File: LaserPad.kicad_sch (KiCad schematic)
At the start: 0 parts

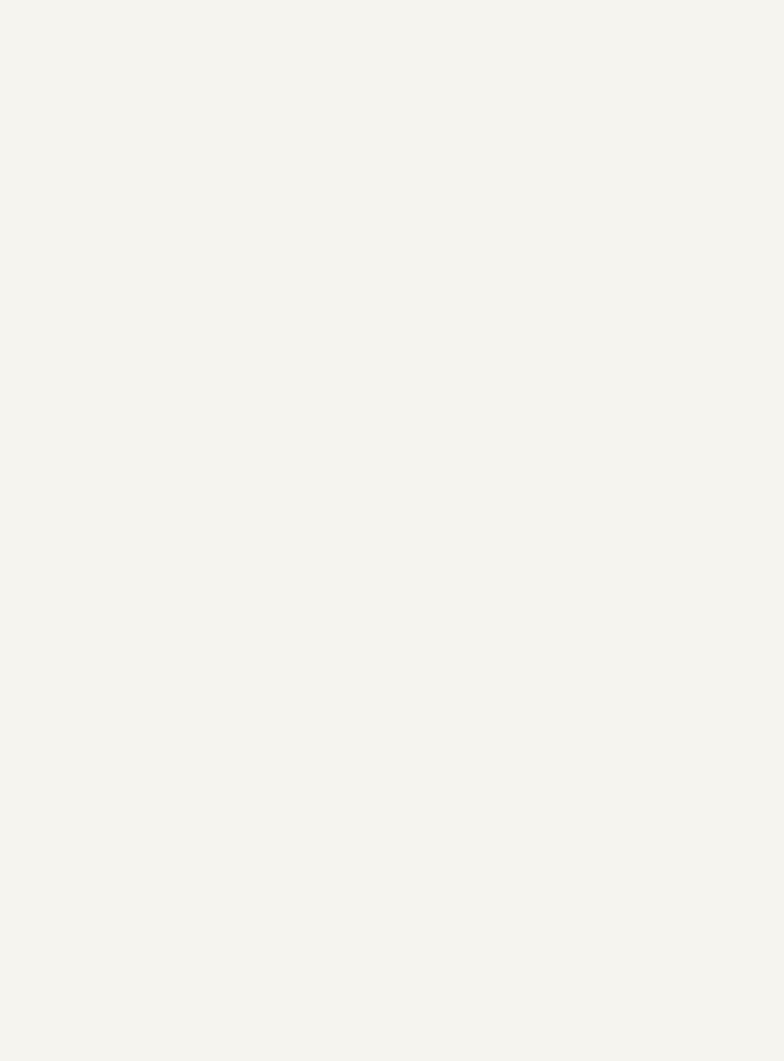
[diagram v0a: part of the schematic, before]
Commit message: Selected MCU and wired up RGB Led Underglow
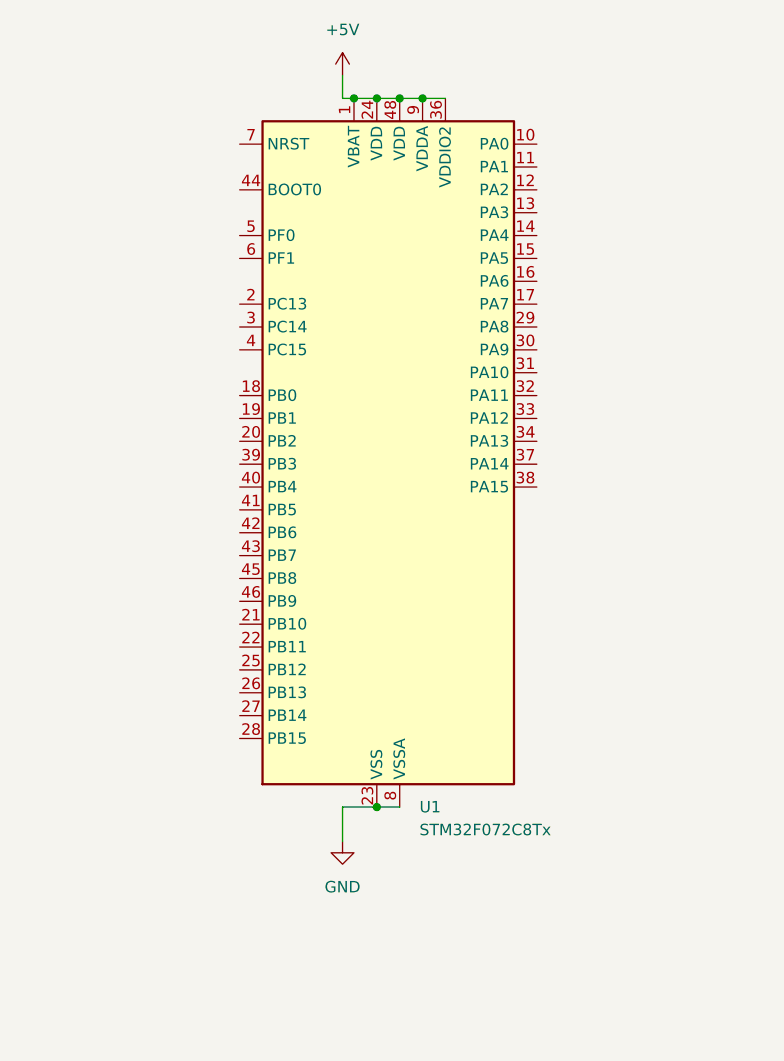
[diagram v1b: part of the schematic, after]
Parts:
- added U1: STM32F072C8Tx, Package_QFP:LQFP-48_7x7mm_P0.5mm, symbol MCU_ST_STM32F0:STM32F072C8Tx
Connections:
- new net +5V: U1.1 (VBAT), U1.24 (VDD), U1.36 (VDDIO2), U1.48 (VDD), U1.9 (VDDA)
- new net GND: U1.23 (VSS), U1.35 (VSS), U1.47 (VSS), U1.8 (VSSA)
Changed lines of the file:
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@@
 (kicad_sch (version 20230121) (generator eeschema)
   (paper "A4")
+  (junction (at 132.08 40.64) (diameter 0) (color 0 0 0 0)
+  )
+  (junction (at 127 119.38) (diameter 0) (color 0 0 0 0)
+  )
+  (junction (at 124.46 40.64) (diameter 0) (color 0 0 0 0)
+  )
+  (junction (at 129.54 40.64) (diameter 0) (color 0 0 0 0)
+  )
+  (junction (at 127 40.64) (diameter 0) (color 0 0 0 0)
+  )
+  (wire (pts (xy 127 119.38) (xy 123.19 119.38))
+    (stroke (width 0) (type default))
+  )
+  (wire (pts (xy 129.54 119.38) (xy 127 119.38))
+    (stroke (width 0) (type default))
+  )
+  (wire (pts (xy 124.46 40.64) (xy 123.19 40.64))
+    (stroke (width 0) (type default))
+  )
+  (wire (pts (xy 129.54 40.64) (xy 127 40.64))
+    (stroke (width 0) (type default))
+  )
+  (wire (pts (xy 123.19 119.38) (xy 123.19 123.19))
+    (stroke (width 0) (type default))
+  )
+  (wire (pts (xy 134.62 40.64) (xy 132.08 40.64))
+    (stroke (width 0) (type default))
+  )
+  (wire (pts (xy 127 40.64) (xy 124.46 40.64))
+    (stroke (width 0) (type default))
+  )
+  (wire (pts (xy 123.19 40.64) (xy 123.19 38.1))
+    (stroke (width 0) (type default))
+  )
+  (wire (pts (xy 132.08 40.64) (xy 129.54 40.64))
+    (stroke (width 0) (type default))
+  )
+  (symbol (lib_id "power:GND") (at 123.19 123.19 0) (unit 1)
+    (in_bom yes) (on_board yes) (dnp no) (fields_autoplaced)
+    (property "Reference" "#PWR01" (at 123.19 129.54 0)
+      (effects (font (size 1.27 1.27)) hide)
+    )
+    (property "Value" "GND" (at 123.19 128.27 0)
+      (effects (font (size 1.27 1.27)))
+    )
+    (property "Footprint" "" (at 123.19 123.19 0)
+      (effects (font (size 1.27 1.27)) hide)
+    )
+    (property "Datasheet" "" (at 123.19 123.19 0)
+      (effects (font (size 1.27 1.27)) hide)
+    )
+    (pin "1")
+    (instances
+      (project "LaserPad"
+        (path "/d1f15120-cbbc-44e4-8f66-361808e417b1"
+          (reference "#PWR01") (unit 1)
+        )
+      )
+    )
+  )
+  (symbol (lib_id "MCU_ST_STM32F0:STM32F072C8Tx") (at 127 81.28 0) (unit 1)
+    (in_bom yes) (on_board yes) (dnp no) (fields_autoplaced)
+    (property "Reference" "U1" (at 131.7341 119.38 0)
+      (effects (font (size 1.27 1.27)) (justify left))
+    )
+    (property "Value" "STM32F072C8Tx" (at 131.7341 121.92 0)
+      (effects (font (size 1.27 1.27)) (justify left))
+    )
+    (property "Footprint" "Package_QFP:LQFP-48_7x7mm_P0.5mm" (at 114.3 116.84 0)
+      (effects (font (size 1.27 1.27)) (justify right) hide)
+    )
+    (property "Datasheet" "https://www.st.com/resource/en/datasheet/stm32f072c8.pdf" (at 127 81.28 0)
+      (effects (font (size 1.27 1.27)) hide)
+    )
+    (pin "24")
+    (pin "16")
+    (pin "19")
+    (pin "12")
+    (pin "21")
+    (pin "23")
+    (pin "28")
+    (pin "3")
+    (pin "13")
+    (pin "32")
+    (pin "31")
+    (pin "2")
+    (pin "34")
+    (pin "35")
+    (pin "41")
+    (pin "48")
+    (pin "6")
+    (pin "29")
+    (pin "26")
+    (pin "44")
+    (pin "46")
+    (pin "40")
+    (pin "47")
+    (pin "14")
+    (pin "20")
+    (pin "42")
+    (pin "43")
+    (pin "18")
+    (pin "8")
+    (pin "11")
+    (pin "22")
+    (pin "27")
+    (pin "9")
+    (pin "30")
+    (pin "25")
+    (pin "10")
+    (pin "38")
+    (pin "45")
+    (pin "5")
+    (pin "15")
+    (pin "36")
+    (pin "1")
+    (pin "17")
+    (pin "37")
+    (pin "4")
+    (pin "7")
+    (pin "33")
+    (pin "39")
+    (instances
+      (project "LaserPad"
+        (path "/d1f15120-cbbc-44e4-8f66-361808e417b1"
+          (reference "U1") (unit 1)
+        )
+      )
+    )
+  )
+  (symbol (lib_id "power:+5V") (at 123.19 38.1 0) (unit 1)
+    (in_bom yes) (on_board yes) (dnp no) (fields_autoplaced)
+    (property "Reference" "#PWR02" (at 123.19 41.91 0)
+      (effects (font (size 1.27 1.27)) hide)
+    )
+    (property "Value" "+5V" (at 123.19 33.02 0)
+      (effects (font (size 1.27 1.27)))
+    )
+    (property "Footprint" "" (at 123.19 38.1 0)
+      (effects (font (size 1.27 1.27)) hide)
+    )
+    (property "Datasheet" "" (at 123.19 38.1 0)
+      (effects (font (size 1.27 1.27)) hide)
+    )
+    (pin "1")
+    (instances
+      (project "LaserPad"
+        (path "/d1f15120-cbbc-44e4-8f66-361808e417b1"
+          (reference "#PWR02") (unit 1)
+        )
+      )
+    )
+  )
   (sheet (at 138.43 153.67) (size 31.75 22.86) (fields_autoplaced)
     (stroke (width 0.1524) (type solid))

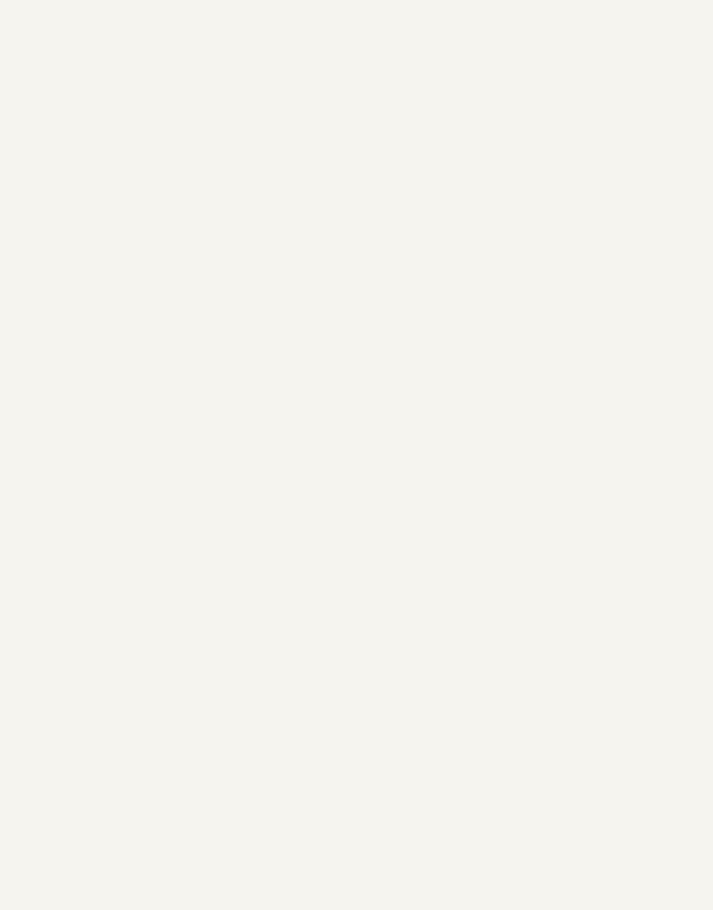
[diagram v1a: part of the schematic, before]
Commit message: Wired USB-C connector in schematic.
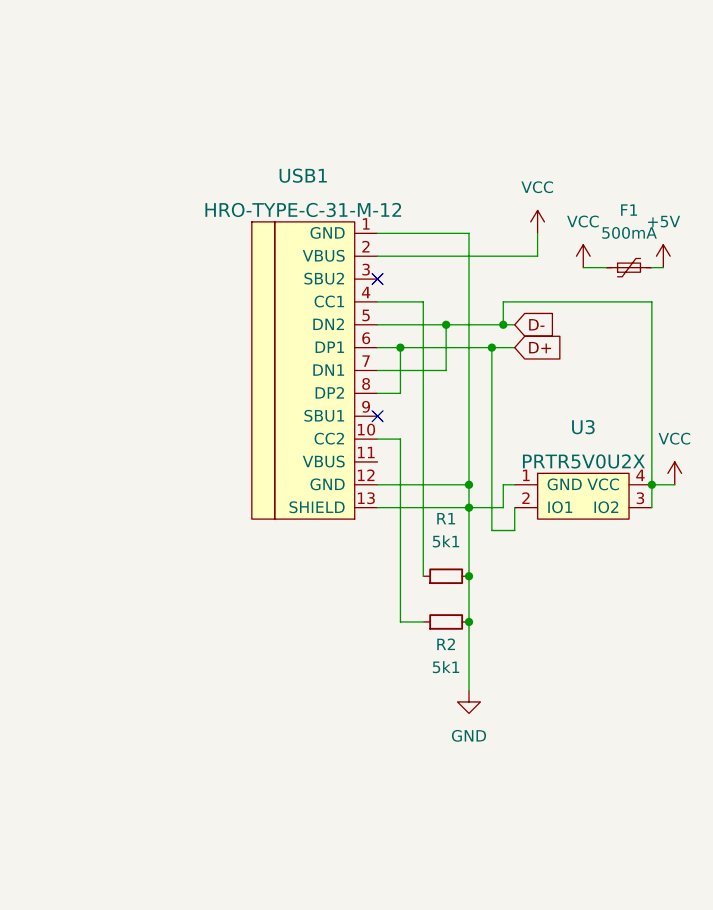
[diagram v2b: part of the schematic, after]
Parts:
- added F1: 500mA, symbol Device:Polyfuse_Small
- added R1, R2: 5k1, symbol Device:R_Small
- added U3: PRTR5V0U2X, symbol random-keyboard-parts:PRTR5V0U2X
- added USB1: HRO-TYPE-C-31-M-12, symbol Type-C:HRO-TYPE-C-31-M-12
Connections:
- net +5V: now also F1.2
- net GND: now also R1.2, R2.2, U3.1 (GND), USB1.1 (GND), USB1.12 (GND), USB1.13 (SHIELD)
- new net: R1.1, USB1.4 (CC1)
- new net: R2.1, USB1.10 (CC2)
- new net D+: U3.2 (IO1), USB1.6 (DP1), USB1.8 (DP2)
- new net VCC: F1.1, U3.3 (IO2), U3.4 (VCC), USB1.2 (VBUS), USB1.5 (DN2), USB1.7 (DN1)
- no-connect marks 0 -> 2

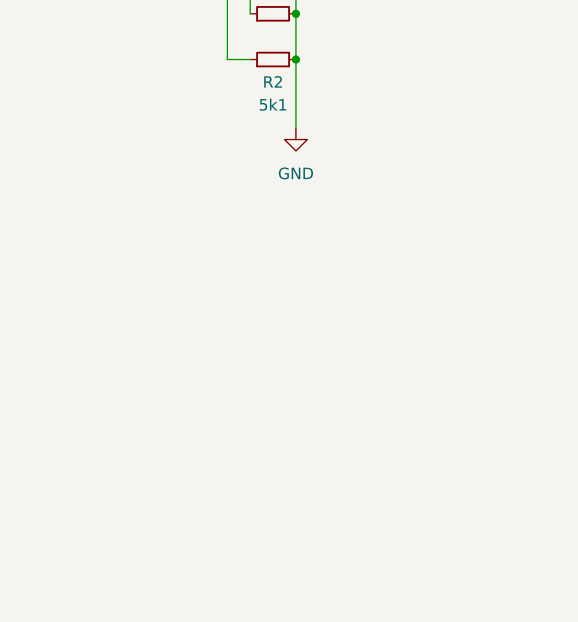
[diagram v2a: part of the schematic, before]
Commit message: added usb power protection
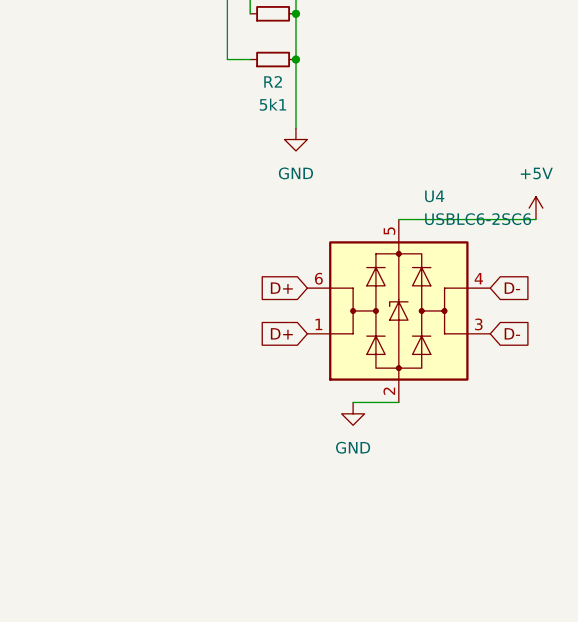
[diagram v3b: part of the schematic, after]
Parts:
- added U4: USBLC6-2SC6, Package_TO_SOT_SMD:SOT-23-6, symbol Power_Protection:USBLC6-2SC6
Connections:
- net +5V: now also U4.5 (VBUS)
- net D+: now also U4.1 (I/O1), U4.6 (I/O1)
- net GND: now also U4.2 (GND)
- net VCC: now also U4.3 (I/O2), U4.4 (I/O2)
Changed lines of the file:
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@@
+    (stroke (width 0) (type default))
+  )
+  (wire (pts (xy 242.57 124.46) (xy 257.81 124.46))
     (stroke (width 0) (type default))
   )
@@
     (stroke (width 0) (type default))
   )
+  (wire (pts (xy 237.49 144.78) (xy 242.57 144.78))
+    (stroke (width 0) (type default))
+  )
   (wire (pts (xy 233.68 96.52) (xy 236.22 96.52))
     (stroke (width 0) (type default))
@@
     (stroke (width 0) (type default))
   )
+  (global_label "D+" (shape input) (at 232.41 137.16 180)
+    (effects (font (size 1.27 1.27)) (justify right))
+    (property "Intersheetrefs" "${INTERSHEET_REFS}" (at 232.41 137.16 0)
+      (effects (font (size 1.27 1.27)) hide)
+    )
+  )
+  (global_label "D-" (shape input) (at 252.73 137.16 0)
+    (effects (font (size 1.27 1.27)) (justify left))
+    (property "Intersheetrefs" "${INTERSHEET_REFS}" (at 252.73 137.16 0)
+      (effects (font (size 1.27 1.27)) hide)
+    )
+  )
   (global_label "D-" (shape input) (at 236.22 73.66 0)
     (effects (font (size 1.27 1.27)) (justify left))
@@
     )
   )
+  (global_label "D-" (shape input) (at 252.73 132.08 0)
+    (effects (font (size 1.27 1.27)) (justify left))
+    (property "Intersheetrefs" "${INTERSHEET_REFS}" (at 252.73 132.08 0)
+      (effects (font (size 1.27 1.27)) hide)
+    )
+  )
   (global_label "D+" (shape input) (at 236.22 76.2 0)
     (effects (font (size 1.27 1.27)) (justify left))
@@
     )
   )
+  (global_label "D+" (shape input) (at 232.41 132.08 180)
+    (effects (font (size 1.27 1.27)) (justify right))
+    (property "Intersheetrefs" "${INTERSHEET_REFS}" (at 232.41 132.08 0)
+      (effects (font (size 1.27 1.27)) hide)
+    )
+  )
   (symbol (lib_id "Device:R_Small") (at 228.6 101.6 90) (unit 1)
     (in_bom yes) (on_board yes) (dnp no)
@@
         (path "/d1f15120-cbbc-44e4-8f66-361808e417b1"
           (reference "#PWR022") (unit 1)
+        )
+      )
+    )
+  )
+  (symbol (lib_id "power:+5V") (at 257.81 124.46 0) (unit 1)
+    (in_bom yes) (on_board yes) (dnp no)
+    (property "Reference" "#PWR028" (at 257.81 128.27 0)
+      (effects (font (size 1.27 1.27)) hide)
+    )
+    (property "Value" "+5V" (at 257.81 119.38 0)
+      (effects (font (size 1.27 1.27)))
+    )
+    (property "Footprint" "" (at 257.81 124.46 0)
+      (effects (font (size 1.27 1.27)) hide)
+    )
+    (property "Datasheet" "" (at 257.81 124.46 0)
+      (effects (font (size 1.27 1.27)) hide)
+    )
+    (pin "1")
+    (instances
+      (project "LaserPad"
+        (path "/d1f15120-cbbc-44e4-8f66-361808e417b1"
+          (reference "#PWR028") (unit 1)
+        )
+      )
+    )
+  )
+  (symbol (lib_id "power:GND") (at 237.49 144.78 0) (unit 1)
+    (in_bom yes) (on_board yes) (dnp no)
+    (property "Reference" "#PWR027" (at 237.49 151.13 0)
+      (effects (font (size 1.27 1.27)) hide)
+    )
+    (property "Value" "GND" (at 237.49 149.86 0)
+      (effects (font (size 1.27 1.27)))
+    )
+    (property "Footprint" "" (at 237.49 144.78 0)
+      (effects (font (size 1.27 1.27)) hide)
+    )
+    (property "Datasheet" "" (at 237.49 144.78 0)
+      (effects (font (size 1.27 1.27)) hide)
+    )
+    (pin "1")
+    (instances
+      (project "LaserPad"
+        (path "/d1f15120-cbbc-44e4-8f66-361808e417b1"
+          (reference "#PWR027") (unit 1)
         )
       )
@@
         )
       )
+    )
+  )
+  (symbol (lib_id "Power_Protection:USBLC6-2SC6") (at 242.57 134.62 0) (unit 1)
+    (in_bom yes) (on_board yes) (dnp no)
+    (property "Reference" "U4" (at 245.3386 121.92 0)
+      (effects (font (size 1.27 1.27)) (justify left))
+    )
+    (property "Value" "USBLC6-2SC6" (at 245.3386 124.46 0)
+      (effects (font (size 1.27 1.27)) (justify left))
+    )
+    (property "Footprint" "Package_TO_SOT_SMD:SOT-23-6" (at 242.57 147.32 0)
+      (effects (font (size 1.27 1.27)) hide)
+    )
+    (property "Datasheet" "https://www.st.com/resource/en/datasheet/usblc6-2.pdf" (at 247.65 125.73 0)
+      (effects (font (size 1.27 1.27)) hide)
+    )
+    (pin "6")
+    (pin "1")
+    (pin "5")
+    (pin "4")
+    (pin "3")
+    (pin "2")
+    (instances
+      (project "LaserPad"
+        (path "/d1f15120-cbbc-44e4-8f66-361808e417b1"
+          (reference "U4") (unit 1)
+        )
+      )

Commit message: did a little organization :/
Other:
- note added: "MCU"
- note added: "USB and USB Power Prot"
- moved on the sheet: F1, R1, R2, U1, U3, U4, USB1

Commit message: idk lol
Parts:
- removed U1: STM32F072C8Tx, Package_QFP:LQFP-48_7x7mm_P0.5mm, symbol MCU_ST_STM32F0:STM32F072C8Tx
- added U1: STM32F072CBTx, Package_QFP:LQFP-48_7x7mm_P0.5mm, symbol MCU_ST_STM32F0:STM32F072CBTx
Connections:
- new net: U1.23 (VSS), U1.35 (VSS), U1.47 (VSS)
